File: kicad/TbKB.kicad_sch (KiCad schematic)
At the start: 141 parts, among them U1 nice_nano

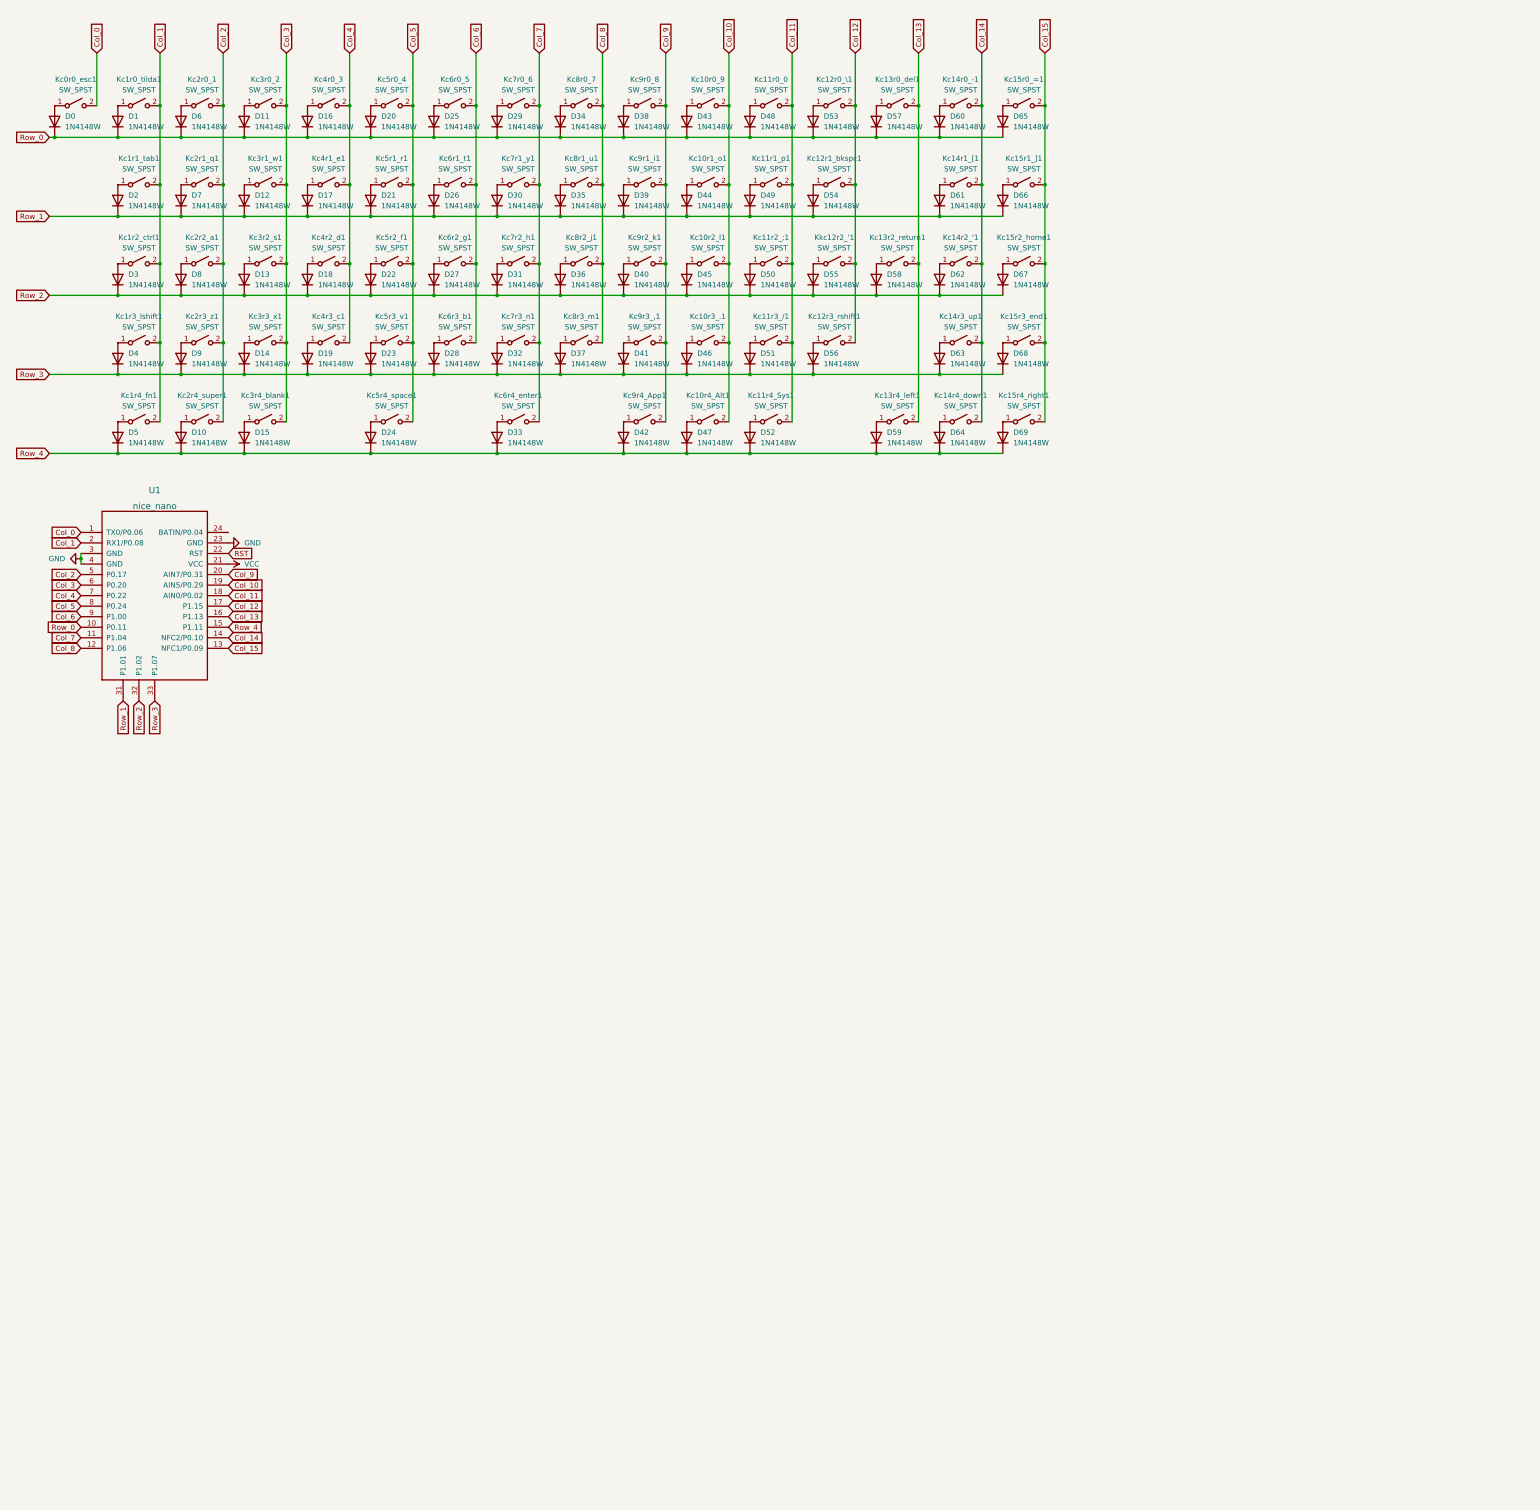
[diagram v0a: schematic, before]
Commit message: arange pcb, switch to RP2040
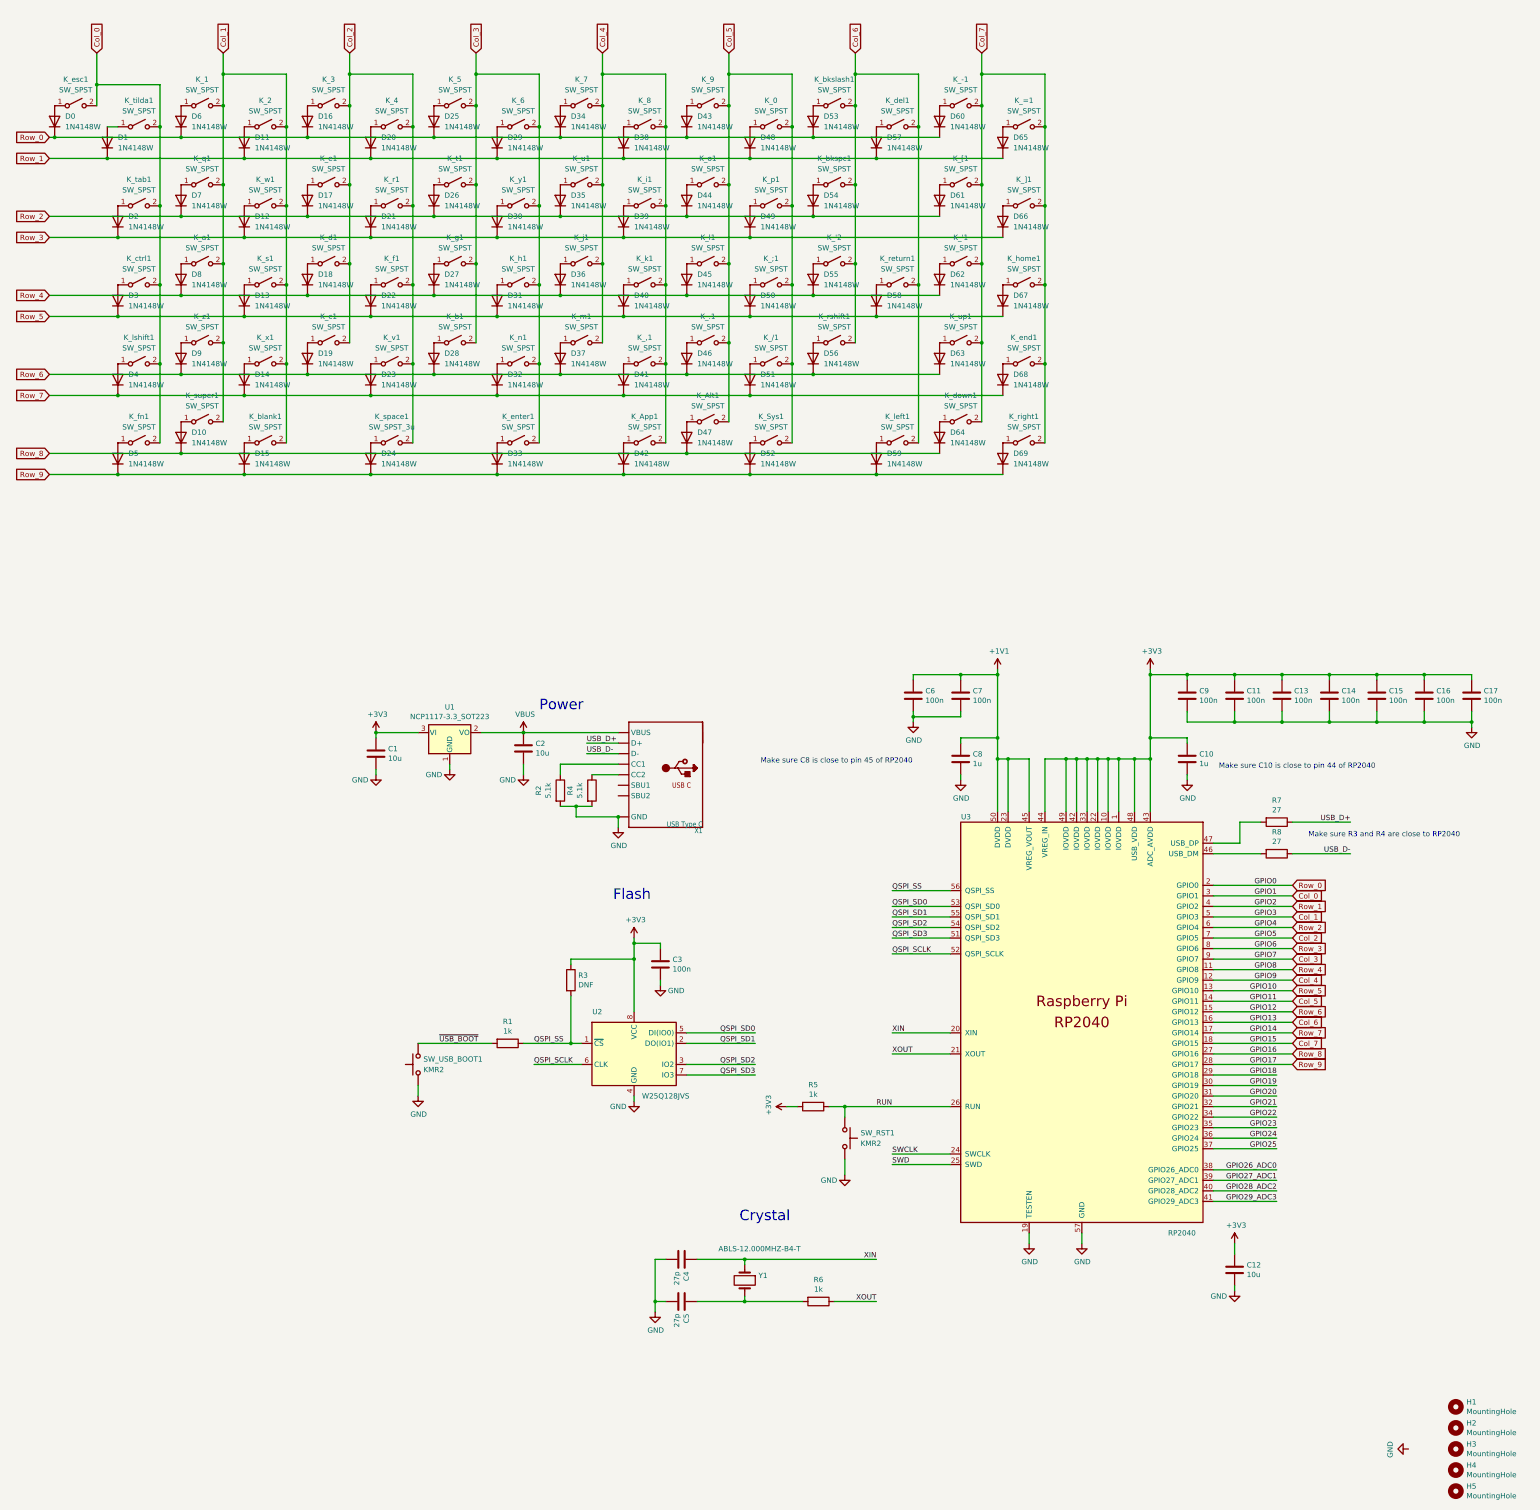
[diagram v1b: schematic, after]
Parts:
- removed U1: nice_nano, nice-nano-kicad:nice_nano, symbol nice_nano:nice_nano
- added C1, C12, C2: 10u, Capacitor_SMD:C_0805_2012Metric, symbol Device:C
- added C10, C8: 1u, Capacitor_SMD:C_0402_1005Metric, symbol Device:C
- added C11, C13, C14, C15, C16, C17, C3, C6, C7, C9: 100n, Capacitor_SMD:C_0402_1005Metric, symbol Device:C
- added C4, C5: 27p, Capacitor_SMD:C_0402_1005Metric, symbol Device:C
- added H1, H2, H3, H4, H5: MountingHole, MountingHole:MountingHole_2.2mm_M2_Pad_Via, symbol Mechanical:MountingHole
- added R1, R5, R6: 1k, Capacitor_SMD:C_0402_1005Metric, symbol Device:R
- added R2, R4: 5.1k, Capacitor_SMD:C_0402_1005Metric, symbol Device:R
- added R3: DNF, Capacitor_SMD:C_0402_1005Metric, symbol Device:R
- added R7, R8: 27, Capacitor_SMD:C_0402_1005Metric, symbol Device:R
- added SW_RST1, SW_USB_BOOT1: KMR2, Button_Switch_SMD:SW_Push_1P1T_NO_CK_KMR2, symbol Switch:SW_Push
- added U1: NCP1117-3.3_SOT223, Package_TO_SOT_SMD:SOT-223-3_TabPin2, symbol Regulator_Linear:NCP1117-3.3_SOT223
- added U2: W25Q128JVS, Package_SO:SOIC-8_5.23x5.23mm_P1.27mm, symbol Memory_Flash:W25Q128JVS
- added U3: RP2040, RP2040_minimal:RP2040-QFN-56, symbol MCU_RaspberryPi_RP2040:RP2040
- added X1: USB Type C, Adafruit Feather RP2040 rev B:USB_C_CUSB31-CFM2AX-01-X, symbol Adafruit Feather RP2040 rev B-eagle-import:USB_C
- added Y1: ABLS-12.000MHZ-B4-T, RP2040_minimal:Crystal_SMD_HC49-US, symbol Device:Crystal
- K_Alt1: renamed from Kc10r4_Alt1; footprint Keebio-Parts:Kailh-PG1350-1.25u -> keyswitches:Kailh_socket_MX_1.25u
- K_bkslash1: renamed from Kc12r0_\1; footprint nice-nano-kicad:nice_nano -> keyswitches:Kailh_socket_MX_1u
- K_bkspc1: renamed from Kc12r1_bkspc1; footprint keyswitches:Kailh_socket_MX_1.75u -> keyswitches:Kailh_socket_MX_2u
- K_ctrl1: renamed from Kc1r2_ctrl1; footprint Keebio-Parts:Kailh-PG1350-1.5u -> keyswitches:Kailh_socket_MX_1.5u
- K_lshift1: renamed from Kc1r3_lshift1; footprint Keebio-Parts:Kailh-PG1350-1.25u -> keyswitches:Kailh_socket_MX_1.25u
- K_return1: renamed from Kc13r2_return1; footprint keyswitches:Kailh_socket_MX_1.75u -> keyswitches:Kailh_socket_MX_1u
- K_rshift1: renamed from Kc12r3_rshift1; footprint keyswitches:Kailh_socket_MX_1.75u -> keyswitches:Kailh_socket_MX_1.5u
- K_space1: renamed from Kc5r4_space1; value SW_SPST -> SW_SPST_3u; footprint keyswitches:Kailh_socket_MX -> keyswitches:Kailh_socket_MX_1u
- K_super1: renamed from Kc2r4_super1; footprint Keebio-Parts:Kailh-PG1350-1.5u -> keyswitches:Kailh_socket_MX_1.5u
- K_tab1: renamed from Kc1r1_tab1; footprint Keebio-Parts:Kailh-PG1350-1.5u -> keyswitches:Kailh_socket_MX_1.5u
- renumbered Kc14r2_'1 to K_'1, Kkc12r2_'1 to K_'2, Kc9r3_,1 to K_,1, Kc14r0_-1 to K_-1, Kc10r3_.1 to K_.1, Kc11r3_/1 to K_/1, Kc11r0_0 to K_0, Kc2r0_1 to K_1, Kc3r0_2 to K_2, Kc4r0_3 to K_3, Kc5r0_4 to K_4, Kc6r0_5 to K_5, Kc7r0_6 to K_6, Kc8r0_7 to K_7, Kc9r0_8 to K_8, Kc10r0_9 to K_9, Kc11r2_;1 to K_;1, Kc15r0_=1 to K_=1, Kc9r4_App1 to K_App1, Kc11r4_Sys1 to K_Sys1, Kc14r1_[1 to K_[1, Kc15r1_]1 to K_]1, Kc2r2_a1 to K_a1, Kc6r3_b1 to K_b1, Kc3r4_blank1 to K_blank1, Kc4r3_c1 to K_c1, Kc4r2_d1 to K_d1, Kc13r0_del1 to K_del1, Kc14r4_down1 to K_down1, Kc4r1_e1 to K_e1, Kc15r3_end1 to K_end1, Kc6r4_enter1 to K_enter1, Kc0r0_esc1 to K_esc1, Kc5r2_f1 to K_f1, Kc1r4_fn1 to K_fn1, Kc6r2_g1 to K_g1, Kc7r2_h1 to K_h1, Kc15r2_home1 to K_home1, Kc9r1_i1 to K_i1, Kc8r2_j1 to K_j1, Kc9r2_k1 to K_k1, Kc10r2_l1 to K_l1, Kc13r4_left1 to K_left1, Kc8r3_m1 to K_m1, Kc7r3_n1 to K_n1, Kc10r1_o1 to K_o1, Kc11r1_p1 to K_p1, Kc2r1_q1 to K_q1, Kc5r1_r1 to K_r1, Kc15r4_right1 to K_right1, Kc3r2_s1 to K_s1, Kc6r1_t1 to K_t1, Kc1r0_tilda1 to K_tilda1, Kc8r1_u1 to K_u1, Kc14r3_up1 to K_up1, Kc5r3_v1 to K_v1, Kc3r1_w1 to K_w1, Kc3r3_x1 to K_x1, Kc7r1_y1 to K_y1, Kc2r3_z1 to K_z1
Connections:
- net Col_10 is gone; now on net Col_5: K_.1.2 (B), K_9.2 (B), K_Alt1.2 (B), K_l1.2 (B), K_o1.2 (B)
- net Col_11 is gone; now on net Col_5: K_/1.2 (B), K_0.2 (B), K_;1.2 (B), K_Sys1.2 (B), K_p1.2 (B)
- net Col_12 is gone; now on net Col_6: K_'2.2 (B), K_bkslash1.2 (B), K_bkspc1.2 (B), K_rshift1.2 (B)
- net Col_13 is gone; now on net Col_6: K_del1.2 (B), K_left1.2 (B), K_return1.2 (B)
- net Col_14 is gone; now on net Col_7: K_'1.2 (B), K_-1.2 (B), K_[1.2 (B), K_down1.2 (B), K_up1.2 (B)
- net Col_15 is gone; now on net Col_7: K_=1.2 (B), K_]1.2 (B), K_end1.2 (B), K_home1.2 (B), K_right1.2 (B)
- net Col_8 is gone; now on net Col_4: K_7.2 (B), K_j1.2 (B), K_m1.2 (B), K_u1.2 (B)
- net Col_9 is gone; now on net Col_4: K_,1.2 (B), K_8.2 (B), K_App1.2 (B), K_i1.2 (B), K_k1.2 (B)
- net Col_0: now also K_ctrl1.2 (B), K_fn1.2 (B), K_lshift1.2 (B), K_tab1.2 (B), K_tilda1.2 (B), U3.3 (GPIO1)
- net Col_1: now also K_1.2 (B), K_2.2 (B), K_a1.2 (B), K_blank1.2 (B), K_q1.2 (B), K_s1.2 (B), K_super1.2 (B), K_w1.2 (B), K_x1.2 (B), K_z1.2 (B), U3.5 (GPIO3); no longer K_ctrl1.2 (B), K_fn1.2 (B), K_lshift1.2 (B), K_tab1.2 (B), K_tilda1.2 (B)
- net Col_2: now also K_3.2 (B), K_4.2 (B), K_c1.2 (B), K_d1.2 (B), K_e1.2 (B), K_f1.2 (B), K_r1.2 (B), K_space1.2 (B), K_v1.2 (B), U3.7 (GPIO5); no longer K_1.2 (B), K_a1.2 (B), K_q1.2 (B), K_super1.2 (B), K_z1.2 (B)
- net Col_3: now also K_5.2 (B), K_6.2 (B), K_b1.2 (B), K_enter1.2 (B), K_g1.2 (B), K_h1.2 (B), K_n1.2 (B), K_t1.2 (B), K_y1.2 (B), U3.9 (GPIO7); no longer K_2.2 (B), K_blank1.2 (B), K_s1.2 (B), K_w1.2 (B), K_x1.2 (B)
- net Col_4: now also U3.12 (GPIO9); no longer K_3.2 (B), K_c1.2 (B), K_d1.2 (B), K_e1.2 (B)
- net Col_5: now also U3.14 (GPIO11); no longer K_4.2 (B), K_f1.2 (B), K_r1.2 (B), K_space1.2 (B), K_v1.2 (B)
- net Col_6: now also U3.16 (GPIO13); no longer K_5.2 (B), K_b1.2 (B), K_g1.2 (B), K_t1.2 (B)
- net Col_7: now also U3.18 (GPIO15); no longer K_6.2 (B), K_enter1.2 (B), K_h1.2 (B), K_n1.2 (B), K_y1.2 (B)
- net GND: now also C1.2, C10.2, C11.2, C12.2, C13.2, C14.2, C15.2, C16.2, C17.2, C2.2, C3.2, C4.2, C5.2, C6.2, C7.2, C8.2, C9.2, R2.2, R4.2, SW_RST1.2, SW_USB_BOOT1.1, U1.1 (GND), U2.4 (GND), U3.19 (TESTEN), U3.57 (GND), X1.A1B12 (GND), X1.B1A12 (GND)
- net Row_0: now also U3.2 (GPIO0); no longer D1.1 (K), D11.1 (K), D20.1 (K), D29.1 (K), D38.1 (K), D48.1 (K), D57.1 (K), D65.1 (K)
- net Row_1: now also D1.1 (K), D11.1 (K), D20.1 (K), D29.1 (K), D38.1 (K), D48.1 (K), D57.1 (K), D65.1 (K), U3.4 (GPIO2); no longer D12.1 (K), D17.1 (K), D2.1 (K), D21.1 (K), D26.1 (K), D30.1 (K), D35.1 (K), D39.1 (K), D44.1 (K), D49.1 (K), D54.1 (K), D61.1 (K), D66.1 (K), D7.1 (K)
- net Row_2: now also D17.1 (K), D26.1 (K), D35.1 (K), D44.1 (K), D54.1 (K), D61.1 (K), D7.1 (K), U3.6 (GPIO4); no longer D13.1 (K), D18.1 (K), D22.1 (K), D27.1 (K), D3.1 (K), D31.1 (K), D36.1 (K), D40.1 (K), D45.1 (K), D50.1 (K), D55.1 (K), D58.1 (K), D62.1 (K), D67.1 (K), D8.1 (K)
- net Row_3: now also D12.1 (K), D2.1 (K), D21.1 (K), D30.1 (K), D39.1 (K), D49.1 (K), D66.1 (K), U3.8 (GPIO6); no longer D14.1 (K), D19.1 (K), D23.1 (K), D28.1 (K), D32.1 (K), D37.1 (K), D4.1 (K), D41.1 (K), D46.1 (K), D51.1 (K), D56.1 (K), D63.1 (K), D68.1 (K), D9.1 (K)
- net Row_4: now also D18.1 (K), D27.1 (K), D36.1 (K), D45.1 (K), D55.1 (K), D62.1 (K), D8.1 (K), U3.11 (GPIO8); no longer D10.1 (K), D15.1 (K), D24.1 (K), D33.1 (K), D42.1 (K), D47.1 (K), D5.1 (K), D52.1 (K), D59.1 (K), D64.1 (K), D69.1 (K)
- new net: R2.1, X1.A5 (CC1)
- new net: R4.1, X1.B5 (CC2)
- new net: R8.2, U3.46 (USB_DM)
- new net: R7.2, U3.47 (USB_DP)
- new net: C5.1, R6.2, Y1.2
- new net +1V1: C6.1, C7.1, C8.1, U3.23 (DVDD), U3.45 (VREG_VOUT), U3.50 (DVDD)
- new net +3V3: C1.1, C10.1, C11.1, C12.1, C13.1, C14.1, C15.1, C16.1, C17.1, C3.1, C9.1, R3.1, R5.2, U1.3 (VI), U2.8 (VCC), U3.1 (IOVDD), U3.10 (IOVDD), U3.22 (IOVDD), U3.33 (IOVDD), U3.42 (IOVDD), U3.43 (ADC_AVDD), U3.44 (VREG_IN), U3.48 (USB_VDD), U3.49 (IOVDD)
- new net GPIO18: U3.29 (GPIO18)
- new net GPIO19: U3.30 (GPIO19)
- new net GPIO20: U3.31 (GPIO20)
- new net GPIO21: U3.32 (GPIO21)
- new net GPIO22: U3.34 (GPIO22)
- new net GPIO23: U3.35 (GPIO23)
- new net GPIO24: U3.36 (GPIO24)
- new net GPIO25: U3.37 (GPIO25)
- new net GPIO26_ADC0: U3.38 (GPIO26_ADC0)
- new net GPIO27_ADC1: U3.39 (GPIO27_ADC1)
- new net GPIO28_ADC2: U3.40 (GPIO28_ADC2)
- new net GPIO29_ADC3: U3.41 (GPIO29_ADC3)
- new net QSPI_SCLK: U2.6 (CLK), U3.52 (QSPI_SCLK)
- new net QSPI_SD0: U2.5 (DI(IO0)), U3.53 (QSPI_SD0)
- new net QSPI_SD1: U2.2 (DO(IO1)), U3.55 (QSPI_SD1)
- new net QSPI_SD2: U2.3 (IO2), U3.54 (QSPI_SD2)
- new net QSPI_SD3: U2.7 (IO3), U3.51 (QSPI_SD3)
- new net QSPI_SS: R1.1, R3.2, U2.1 (~{CS}), U3.56 (QSPI_SS)
- new net RUN: R5.1, SW_RST1.1, U3.26 (RUN)
- new net Row_5: D13.1 (K), D22.1 (K), D3.1 (K), D31.1 (K), D40.1 (K), D50.1 (K), D58.1 (K), D67.1 (K), U3.13 (GPIO10)
- new net Row_6: D19.1 (K), D28.1 (K), D37.1 (K), D46.1 (K), D56.1 (K), D63.1 (K), D9.1 (K), U3.15 (GPIO12)
- new net Row_7: D14.1 (K), D23.1 (K), D32.1 (K), D4.1 (K), D41.1 (K), D51.1 (K), D68.1 (K), U3.17 (GPIO14)
- new net Row_8: D10.1 (K), D47.1 (K), D64.1 (K), U3.27 (GPIO16)
- new net Row_9: D15.1 (K), D24.1 (K), D33.1 (K), D42.1 (K), D5.1 (K), D52.1 (K), D59.1 (K), D69.1 (K), U3.28 (GPIO17)
- new net SWCLK: U3.24 (SWCLK)
- new net SWD: U3.25 (SWD)
- new net USB_D+: R7.1, X1.A6 (D+), X1.B6 (D+)
- new net USB_D-: R8.1, X1.A7 (D-), X1.B7 (D-)
- new net VBUS: C2.1, U1.2 (VO), X1.A4B9 (VBUS), X1.B4A9 (VBUS)
- new net XIN: C4.1, U3.20 (XIN), Y1.1
- new net XOUT: R6.1, U3.21 (XOUT)
- new net ~{USB_BOOT}: R1.2, SW_USB_BOOT1.2
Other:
- note added: "Crystal"
- note added: "Flash"
- note added: "Make sure C10 is close to pin 44 of RP2040"
- note added: "Make sure C8 is close to pin 45 of RP2040"
- note added: "Make sure R3 and R4 are close to RP2040"
- note added: "Power"
- moved on the sheet: D1, D11, D12, D13, D14, D15, D2, D20, D21, D22, D23, D24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

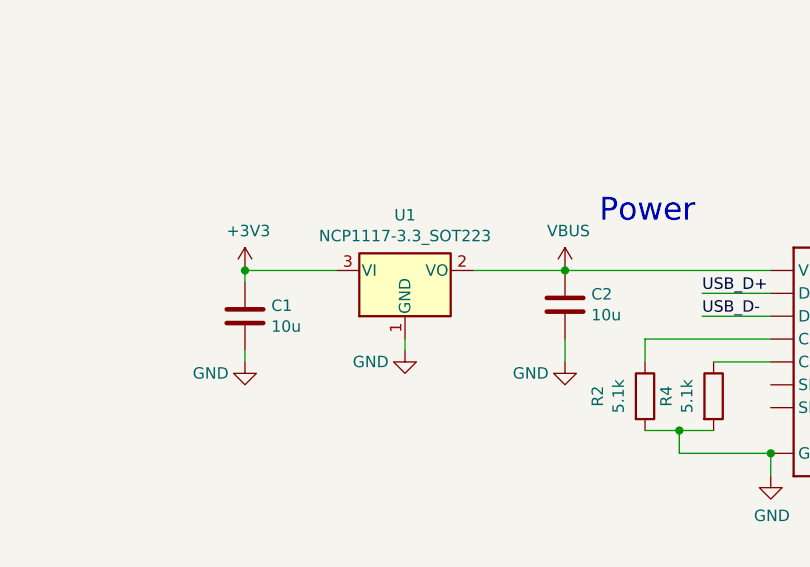
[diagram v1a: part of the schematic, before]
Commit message: switched to smaller crystal, other switch fixes
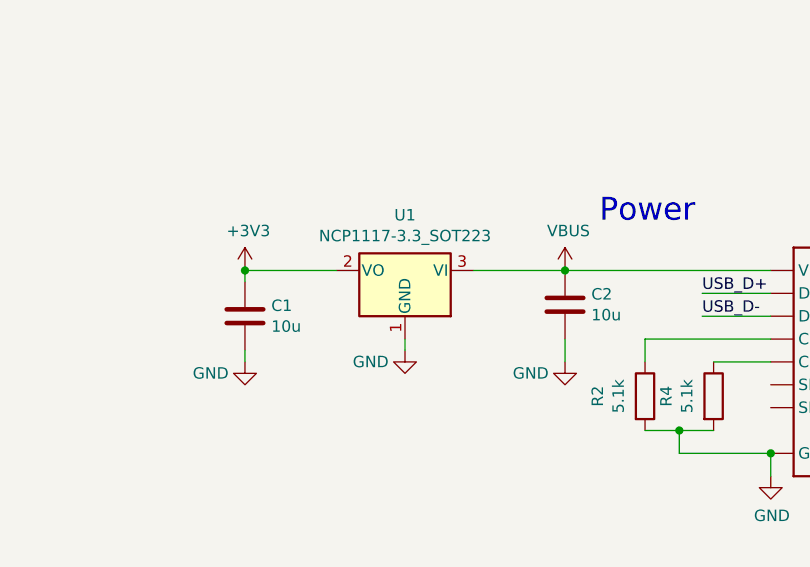
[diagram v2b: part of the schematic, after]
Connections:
- net +3V3: now also U1.2 (VO); no longer U1.3 (VI)
- net VBUS: now also U1.3 (VI); no longer U1.2 (VO)
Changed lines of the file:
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@@
     (pin "2")
   )
-  (symbol (lib_id "Regulator_Linear:NCP1117-3.3_SOT223") (at 121.92 189.23 0) (unit 1)
+  (symbol (lib_id "Regulator_Linear:NCP1117-3.3_SOT223") (at 121.92 189.23 0) (mirror y) (unit 1)
     (in_bom yes) (on_board yes)
     (property "Reference" "U1" (id 0) (at 121.92 183.0832 0))
@@
       (effects (font (size 1.27 1.27)) hide)
     )
-    (property "Datasheet" "http://www.onsemi.com/pub_link/Collateral/NCP1117-D.PDF" (id 3) (at 124.46 195.58 0)
+    (property "Datasheet" "http://www.onsemi.com/pub_link/Collateral/NCP1117-D.PDF" (id 3) (at 119.38 195.58 0)
       (effects (font (size 1.27 1.27)) hide)
     )

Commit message: Added Addressable RGB leds, ancilarry capacitors, and edge cuts
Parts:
- added C18, C19, C20, C21, C22, C23, C24, C25, C26, C27, C28, C29, C30, C31, C32, C33, C34, C35, C36, C37, C38, C39, C40, C41, C42, C43, C44, C45, C46, C47, C48, C49, C50, C51, C52, C53, C54, C55, C56, C57, C58, C59, C60, C61, C62, C63, C64, C65, C66, C67, C68, C69, C70, C71, C72, C73, C74, C75, C76, C77, C78, C79, C80, C81, C82, C83, C84, C85, C86, C87: 100n, Capacitor_SMD:C_0402_1005Metric, symbol Device:C
- added D100, D101, D102, D103, D104, D105, D106, D107, D108, D109, D110, D111, D112, D113, D114, D115, D116, D117, D118, D119, D120, D121, D122, D123, D124, D125, D126, D127, D128, D129, D130, D131, D132, D133, D134, D135, D136, D137, D138, D139, D70, D71, D72, D73, D74, D75, D76, D77, D78, D79, D80, D81, D82, D83, D84, D85, D86, D87, D88, D89, D90, D91, D92, D93, D94, D95, D96, D97, D98, D99: SK6812MINI, LED_SMD:LED_SK6812MINI_PLCC4_3.5x3.5mm_P1.75mm, symbol LED:SK6812MINI
- added RV1, RV2, RV3: R_Potentiometer_US, potentiometers:Potentiometer_Bourns_PTA6043_Single_Slide, symbol Device:R_Potentiometer_US
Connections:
- net +3V3: now also C18.2, C19.2, C20.2, C21.2, C22.2, C23.2, C24.2, C25.2, C26.2, C27.2, C28.2, C29.2, C30.2, C31.2, C32.2, C33.2, C34.2, C35.2, C36.2, C37.2, C38.2, C39.2, C40.2, C41.2, C42.2, C43.2, C44.2, C45.2, C46.2, C47.2, C48.2, C49.2, C50.2, C51.2, C52.2, C53.2, C54.2, C55.2, C56.2, C57.2, C58.2, C59.2, C60.2, C61.2, C62.2, C63.2, C64.2, C65.2, C66.2, C67.2, C68.2, C69.2, C70.2, C71.2, C72.2, C73.2, C74.2, C75.2, C76.2, C77.2, C78.2, C79.2, C80.2, C81.2, C82.2, C83.2, C84.2, C85.2, C86.2, C87.2, D100.4 (VDD), D101.4 (VDD), D102.4 (VDD), D103.4 (VDD), D104.4 (VDD), D105.4 (VDD), D106.4 (VDD), D107.4 (VDD), D108.4 (VDD), D109.4 (VDD), D110.4 (VDD), D111.4 (VDD), D112.4 (VDD), D113.4 (VDD), D114.4 (VDD), D115.4 (VDD), D116.4 (VDD), D117.4 (VDD), D118.4 (VDD), D119.4 (VDD), D120.4 (VDD), D121.4 (VDD), D122.4 (VDD), D123.4 (VDD), D124.4 (VDD), D125.4 (VDD), D126.4 (VDD), D127.4 (VDD), D128.4 (VDD), D129.4 (VDD), D130.4 (VDD), D131.4 (VDD), D132.4 (VDD), D133.4 (VDD), D134.4 (VDD), D135.4 (VDD), D136.4 (VDD), D137.4 (VDD), D138.4 (VDD), D139.4 (VDD), D70.4 (VDD), D71.4 (VDD), D72.4 (VDD), D73.4 (VDD), D74.4 (VDD), D75.4 (VDD), D76.4 (VDD), D77.4 (VDD), D78.4 (VDD), D79.4 (VDD), D80.4 (VDD), D81.4 (VDD), D82.4 (VDD), D83.4 (VDD), D84.4 (VDD), D85.4 (VDD), D86.4 (VDD), D87.4 (VDD), D88.4 (VDD), D89.4 (VDD), D90.4 (VDD), D91.4 (VDD), D92.4 (VDD), D93.4 (VDD), D94.4 (VDD), D95.4 (VDD), D96.4 (VDD), D97.4 (VDD), D98.4 (VDD), D99.4 (VDD), RV1.1, RV2.1, RV3.1
- net GND: now also C18.1, C19.1, C20.1, C21.1, C22.1, C23.1, C24.1, C25.1, C26.1, C27.1, C28.1, C29.1, C30.1, C31.1, C32.1, C33.1, C34.1, C35.1, C36.1, C37.1, C38.1, C39.1, C40.1, C41.1, C42.1, C43.1, C44.1, C45.1, C46.1, C47.1, C48.1, C49.1, C50.1, C51.1, C52.1, C53.1, C54.1, C55.1, C56.1, C57.1, C58.1, C59.1, C60.1, C61.1, C62.1, C63.1, C64.1, C65.1, C66.1, C67.1, C68.1, C69.1, C70.1, C71.1, C72.1, C73.1, C74.1, C75.1, C76.1, C77.1, C78.1, C79.1, C80.1, C81.1, C82.1, C83.1, C84.1, C85.1, C86.1, C87.1, D100.2 (VSS), D101.2 (VSS), D102.2 (VSS), D103.2 (VSS), D104.2 (VSS), D105.2 (VSS), D106.2 (VSS), D107.2 (VSS), D108.2 (VSS), D109.2 (VSS), D110.2 (VSS), D111.2 (VSS), D112.2 (VSS), D113.2 (VSS), D114.2 (VSS), D115.2 (VSS), D116.2 (VSS), D117.2 (VSS), D118.2 (VSS), D119.2 (VSS), D120.2 (VSS), D121.2 (VSS), D122.2 (VSS), D123.2 (VSS), D124.2 (VSS), D125.2 (VSS), D126.2 (VSS), D127.2 (VSS), D128.2 (VSS), D129.2 (VSS), D130.2 (VSS), D131.2 (VSS), D132.2 (VSS), D133.2 (VSS), D134.2 (VSS), D135.2 (VSS), D136.2 (VSS), D137.2 (VSS), D138.2 (VSS), D139.2 (VSS), D70.2 (VSS), D71.2 (VSS), D72.2 (VSS), D73.2 (VSS), D74.2 (VSS), D75.2 (VSS), D76.2 (VSS), D77.2 (VSS), D78.2 (VSS), D79.2 (VSS), D80.2 (VSS), D81.2 (VSS), D82.2 (VSS), D83.2 (VSS), D84.2 (VSS), D85.2 (VSS), D86.2 (VSS), D87.2 (VSS), D88.2 (VSS), D89.2 (VSS), D90.2 (VSS), D91.2 (VSS), D92.2 (VSS), D93.2 (VSS), D94.2 (VSS), D95.2 (VSS), D96.2 (VSS), D97.2 (VSS), D98.2 (VSS), D99.2 (VSS), RV1.3, RV2.3, RV3.3
- net GPIO25 renamed LED_ARRAY
- net LED_ARRAY: now also D70.3 (DIN)
- net GPIO27_ADC1 renamed RV1
- net RV1: now also RV1.2
- net GPIO28_ADC2 renamed RV2
- net RV2: now also RV2.2
- net GPIO29_ADC3 renamed RV3
- net RV3: now also RV3.2
- new net: D134.1 (DOUT), D75.3 (DIN)
- new net: D124.1 (DOUT), D134.3 (DIN)
- new net: D115.1 (DOUT), D125.3 (DIN)
- new net: D105.1 (DOUT), D115.3 (DIN)
- new net: D137.1 (DOUT), D78.3 (DIN)
- new net: D127.1 (DOUT), D137.3 (DIN)
- new net: D119.1 (DOUT), D129.3 (DIN)
- new net: D109.1 (DOUT), D119.3 (DIN)
- new net: D104.3 (DIN), D94.1 (DOUT)
- new net: D84.1 (DOUT), D94.3 (DIN)
- new net: D82.1 (DOUT), D92.3 (DIN)
- new net: D72.1 (DOUT), D82.3 (DIN)
- new net: D129.1 (DOUT), D139.3 (DIN)
- new net: D135.1 (DOUT), D76.3 (DIN)
- new net: D125.1 (DOUT), D135.3 (DIN)
- new net: D117.1 (DOUT), D127.3 (DIN)
- new net: D107.1 (DOUT), D117.3 (DIN)
- new net: D121.1 (DOUT), D131.3 (DIN)
- new net: D111.1 (DOUT), D121.3 (DIN)
- new net: D116.1 (DOUT), D126.3 (DIN)
- new net: D106.1 (DOUT), D116.3 (DIN)
- new net: D130.1 (DOUT), D71.3 (DIN)
- new net: D120.1 (DOUT), D130.3 (DIN)
- new net: D131.1 (DOUT), D72.3 (DIN)
- new net: D100.1 (DOUT), D110.3 (DIN)
- new net: D100.3 (DIN), D90.1 (DOUT)
- new net: D75.1 (DOUT), D85.3 (DIN)
- new net: D118.1 (DOUT), D128.3 (DIN)
- new net: D108.1 (DOUT), D118.3 (DIN)
- new net: D132.1 (DOUT), D73.3 (DIN)
- new net: D122.1 (DOUT), D132.3 (DIN)
- new net: D104.1 (DOUT), D114.3 (DIN)
- new net: D110.1 (DOUT), D120.3 (DIN)
- new net: D107.3 (DIN), D97.1 (DOUT)
- new net: D88.1 (DOUT), D98.3 (DIN)
- new net: D78.1 (DOUT), D88.3 (DIN)
- new net: D83.1 (DOUT), D93.3 (DIN)
- new net: D73.1 (DOUT), D83.3 (DIN)
- new net: D114.1 (DOUT), D124.3 (DIN)
- new net: D85.1 (DOUT), D95.3 (DIN)
- new net: D108.3 (DIN), D98.1 (DOUT)
- new net: D101.1 (DOUT), D111.3 (DIN)
- new net: D101.3 (DIN), D91.1 (DOUT)
- new net: D109.3 (DIN), D99.1 (DOUT)
- new net: D89.1 (DOUT), D99.3 (DIN)
- new net: D87.1 (DOUT), D97.3 (DIN)
- new net: D77.1 (DOUT), D87.3 (DIN)
- new net: D81.1 (DOUT), D91.3 (DIN)
- new net: D71.1 (DOUT), D81.3 (DIN)
- new net: D126.1 (DOUT), D136.3 (DIN)
- new net: D79.1 (DOUT), D89.3 (DIN)
- new net: D113.1 (DOUT), D123.3 (DIN)
- new net: D103.1 (DOUT), D113.3 (DIN)
- new net: D112.1 (DOUT), D122.3 (DIN)
- new net: D105.3 (DIN), D95.1 (DOUT)
- new net: D138.1 (DOUT), D79.3 (DIN)
- new net: D128.1 (DOUT), D138.3 (DIN)
- new net: D103.3 (DIN), D93.1 (DOUT)
- new net: D86.1 (DOUT), D96.3 (DIN)
- new net: D76.1 (DOUT), D86.3 (DIN)
- new net: D136.1 (DOUT), D77.3 (DIN)
- new net: D102.1 (DOUT), D112.3 (DIN)
- new net: D70.1 (DOUT), D80.3 (DIN)
- new net: D74.1 (DOUT), D84.3 (DIN)
- new net: D123.1 (DOUT), D133.3 (DIN)
- new net: D80.1 (DOUT), D90.3 (DIN)
- new net: D102.3 (DIN), D92.1 (DOUT)
- new net: D133.1 (DOUT), D74.3 (DIN)
- new net: D106.3 (DIN), D96.1 (DOUT)
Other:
- moved on the sheet: C1, C10, C11, C12, C13, C14, C15, C16, C17, C2, C3, C4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
